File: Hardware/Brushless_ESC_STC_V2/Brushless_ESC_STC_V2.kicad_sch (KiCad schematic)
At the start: 7 parts

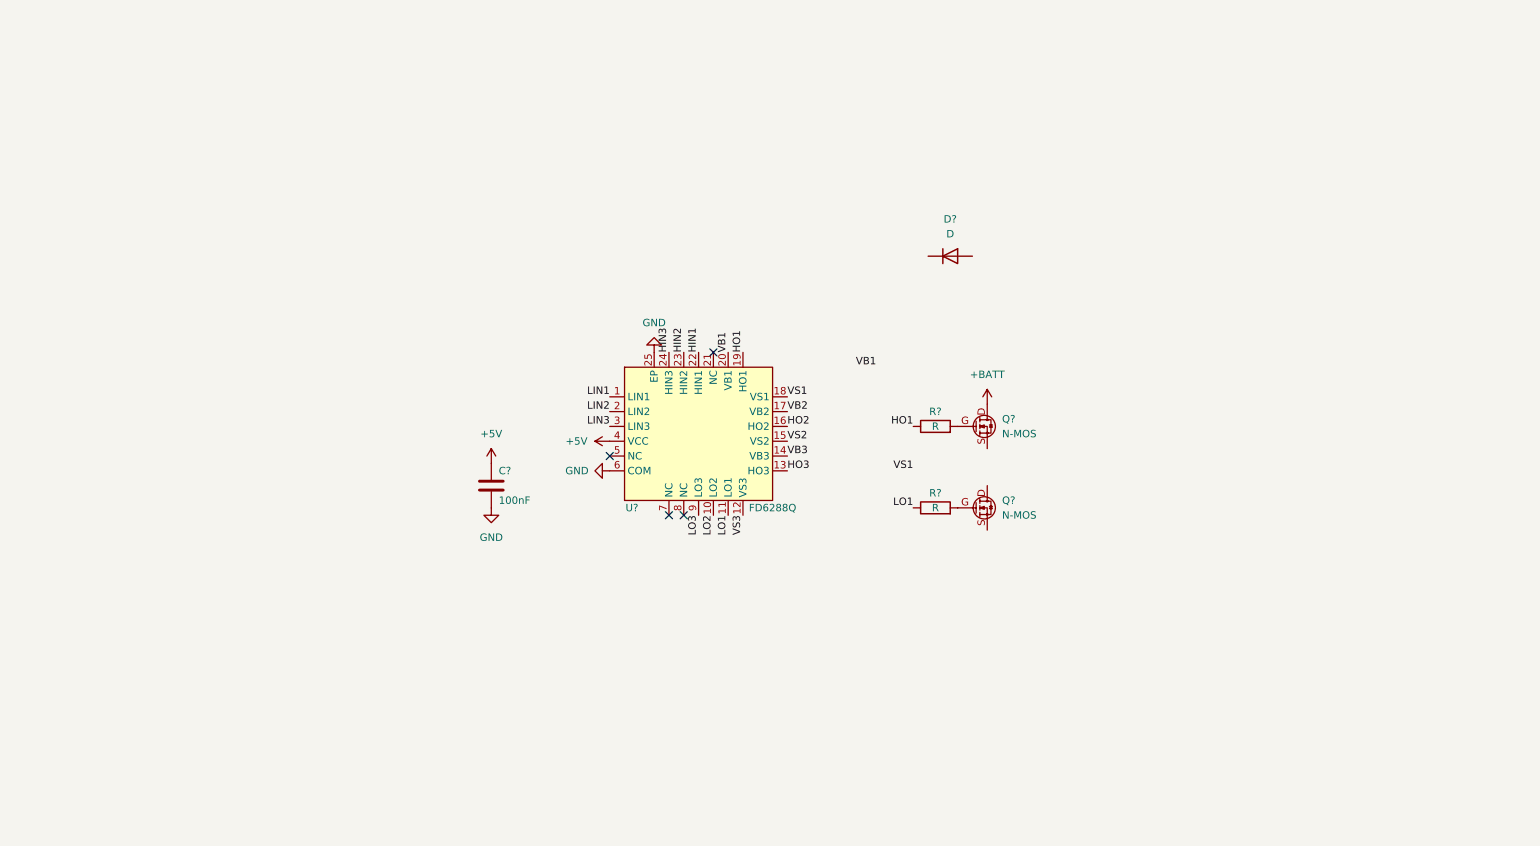
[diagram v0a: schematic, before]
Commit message: 增加STC8H1K17版本电调PCB初版设计文件，尚未完成检查
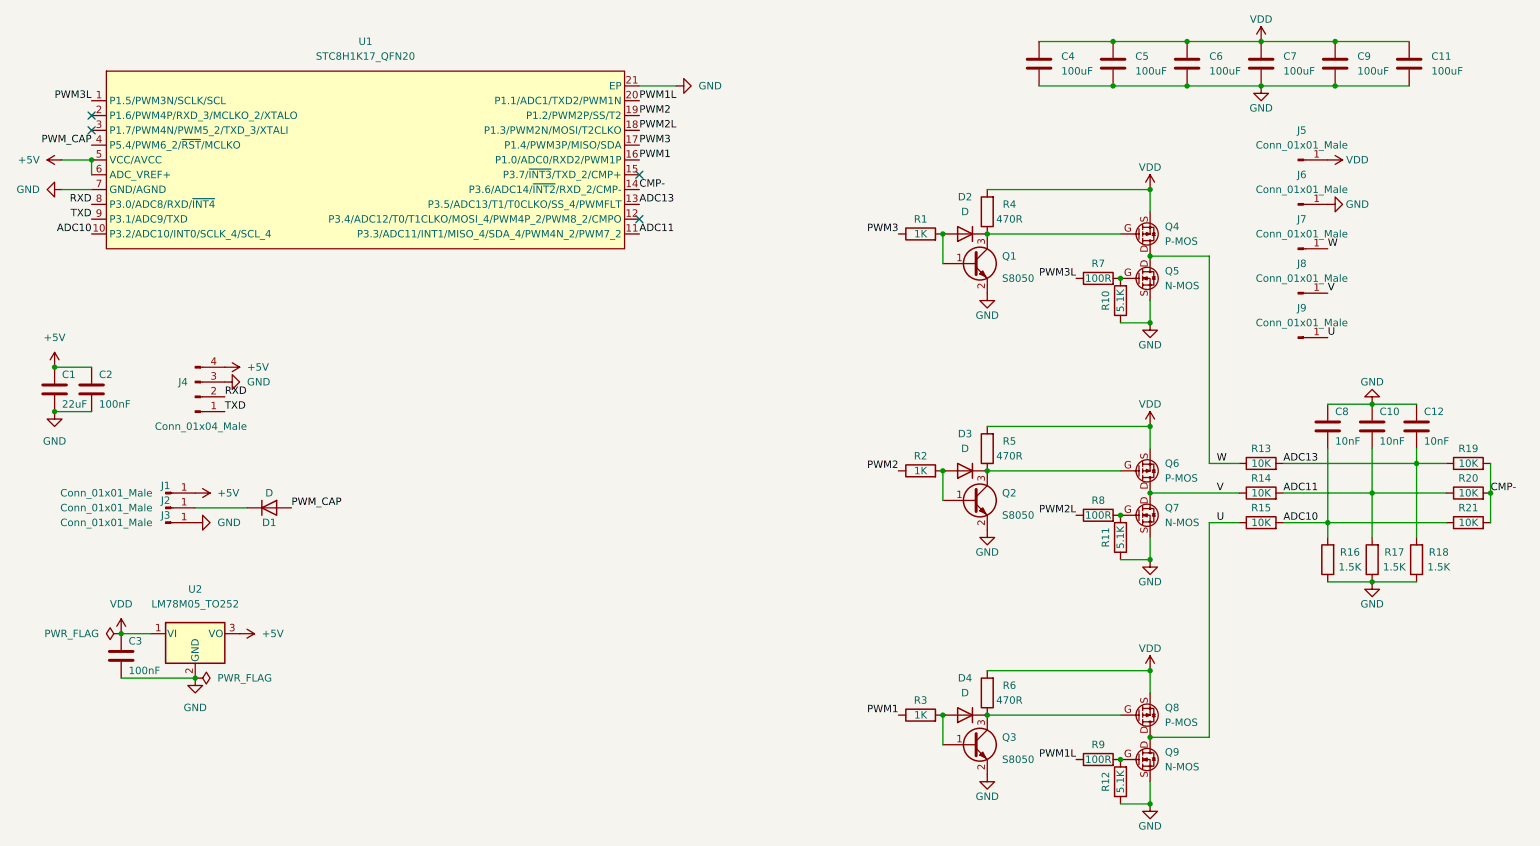
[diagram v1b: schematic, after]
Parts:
- removed C?: 100nF, symbol Device:C
- removed D?: D, symbol Device:D
- removed Q? (x2): N-MOS, symbol Del_Schlib:N-MOS
- removed R? (x2): R, symbol Device:R
- removed U?: FD6288Q, Package_DFN_QFN:QFN-24-1EP_4x4mm_P0.5mm_EP2.6x2.6mm, symbol Del_Schlib:FD6288Q
- added C1: 22uF, Capacitor_SMD:C_1206_3216Metric, symbol Device:C
- added C10, C12, C8: 10nF, Capacitor_SMD:C_0603_1608Metric_Pad1.08x0.95mm_HandSolder, symbol Device:C
- added C11, C4, C5, C6, C7, C9: 100uF, Capacitor_SMD:C_1210_3225Metric, symbol Device:C
- added C2, C3: 100nF, Capacitor_SMD:C_0603_1608Metric_Pad1.08x0.95mm_HandSolder, symbol Device:C
- added D1, D2, D3, D4: D, Diode_SMD:D_SOD-123, symbol Device:D
- added J1, J2, J3, J5, J6, J7, J8, J9: Conn_01x01_Male, Del:PAD_RECT, symbol Connector:Conn_01x01_Male
- added J4: Conn_01x04_Male, Del:SH1.0mm_4P_WT, symbol Connector:Conn_01x04_Male
- added Q1, Q2, Q3: S8050, Package_TO_SOT_SMD:SOT-23, symbol Device:Q_NPN_BEC
- added Q4, Q6, Q8: P-MOS, Del:P-MOS-TO-252-2, symbol Del_Schlib:P-MOS
- added Q5, Q7, Q9: N-MOS, Del:N-MOS-TO-252-2, symbol Del_Schlib:N-MOS
- added R1, R2, R3: 1K, Resistor_SMD:R_0603_1608Metric_Pad0.98x0.95mm_HandSolder, symbol Device:R
- added R10, R11, R12: 5.1K, Resistor_SMD:R_0603_1608Metric_Pad0.98x0.95mm_HandSolder, symbol Device:R
- added R13, R14, R15, R19, R20, R21: 10K, Resistor_SMD:R_0603_1608Metric_Pad0.98x0.95mm_HandSolder, symbol Device:R
- added R16, R17, R18: 1.5K, Resistor_SMD:R_0603_1608Metric_Pad0.98x0.95mm_HandSolder, symbol Device:R
- added R4, R5, R6: 470R, Resistor_SMD:R_0603_1608Metric_Pad0.98x0.95mm_HandSolder, symbol Device:R
- added R7, R8, R9: 100R, Resistor_SMD:R_0603_1608Metric_Pad0.98x0.95mm_HandSolder, symbol Device:R
- added U1: STC8H1K17_QFN20, Package_DFN_QFN:QFN-20-1EP_3x3mm_P0.4mm_EP1.65x1.65mm, symbol Del_Schlib:STC8H1K17_QFN20
- added U2: LM78M05_TO252, Package_TO_SOT_SMD:TO-252-2, symbol Regulator_Linear:LM78M05_TO252
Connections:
- net +5V: now also C1.1, C2.1, J1.1 (Pin_1), J4.4 (Pin_4), U1.5 (VCC/AVCC), U1.6 (ADC_VREF+), U2.3 (VO)
- net GND: now also C1.2, C10.1, C11.2, C12.1, C2.2, C3.2, C4.2, C5.2, C6.2, C7.2, C8.1, C9.2, J3.1 (Pin_1), J4.3 (Pin_3), J6.1 (Pin_1), Q1.2 (E), Q2.2 (E), Q3.2 (E), Q5.S, Q7.S, Q9.S, R10.1, R11.1, R12.1, R16.1, R17.1, R18.1, U1.21 (EP), U1.7 (GND/AGND), U2.2 (GND)
- new net: D2.2 (A), Q1.1 (B), R1.2
- new net: Q7.G, R11.2, R8.2
- new net: D2.1 (K), Q1.3 (C), Q4.G, R4.1
- new net: D4.1 (K), Q3.3 (C), Q8.G, R6.1
- new net: D1.1 (K), J2.1 (Pin_1)
- new net: D4.2 (A), Q3.1 (B), R3.2
- new net: Q5.G, R10.2, R7.2
- new net: D3.1 (K), Q2.3 (C), Q6.G, R5.1
- new net: Q9.G, R12.2, R9.2
- new net: D3.2 (A), Q2.1 (B), R2.2
- new net ADC10: C8.2, R15.2, R16.2, R21.1, U1.10 (P3.2/ADC10/INT0/SCLK_4/SCL_4)
- new net ADC11: C10.2, R14.2, R17.2, R20.1, U1.11 (P3.3/ADC11/INT1/MISO_4/SDA_4/PWM4N_2/PWM7_2)
- new net ADC13: C12.2, R13.2, R18.2, R19.1, U1.13 (P3.5/ADC13/T1/T0CLKO/SS_4/PWMFLT)
- new net CMP-: R19.2, R20.2, R21.2, U1.14 (P3.6/ADC14/~{INT2}/RXD_2/CMP-)
- new net PWM1: R3.1, U1.16 (P1.0/ADC0/RXD2/PWM1P)
- new net PWM1L: R9.1, U1.20 (P1.1/ADC1/TXD2/PWM1N)
- new net PWM2: R2.1, U1.19 (P1.2/PWM2P/SS/T2)
- new net PWM2L: R8.1, U1.18 (P1.3/PWM2N/MOSI/T2CLKO)
- new net PWM3: R1.1, U1.17 (P1.4/PWM3P/MISO/SDA)
- new net PWM3L: R7.1, U1.1 (P1.5/PWM3N/SCLK/SCL)
- new net PWM_CAP: D1.2 (A), U1.4 (P5.4/PWM6_2/~{RST}/MCLKO)
- new net RXD: J4.2 (Pin_2), U1.8 (P3.0/ADC8/RXD/~{INT4})
- new net TXD: J4.1 (Pin_1), U1.9 (P3.1/ADC9/TXD)
- new net U: J9.1 (Pin_1), Q8.D, Q9.D, R15.1
- new net V: J8.1 (Pin_1), Q6.D, Q7.D, R14.1
- new net VDD: C11.1, C3.1, C4.1, C5.1, C6.1, C7.1, C9.1, J5.1 (Pin_1), Q4.S, Q6.S, Q8.S, R4.2, R5.2, R6.2, U2.1 (VI)
- new net W: J7.1 (Pin_1), Q4.D, Q5.D, R13.1
